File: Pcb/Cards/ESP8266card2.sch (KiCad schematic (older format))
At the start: 13 parts, among them J1 CONN_01X02, J2 CONN_02X06, P1 ESP-Programming-FTDI, U1 SN74AHC1G08, U2 ESP-12E/F, X1 HOLE

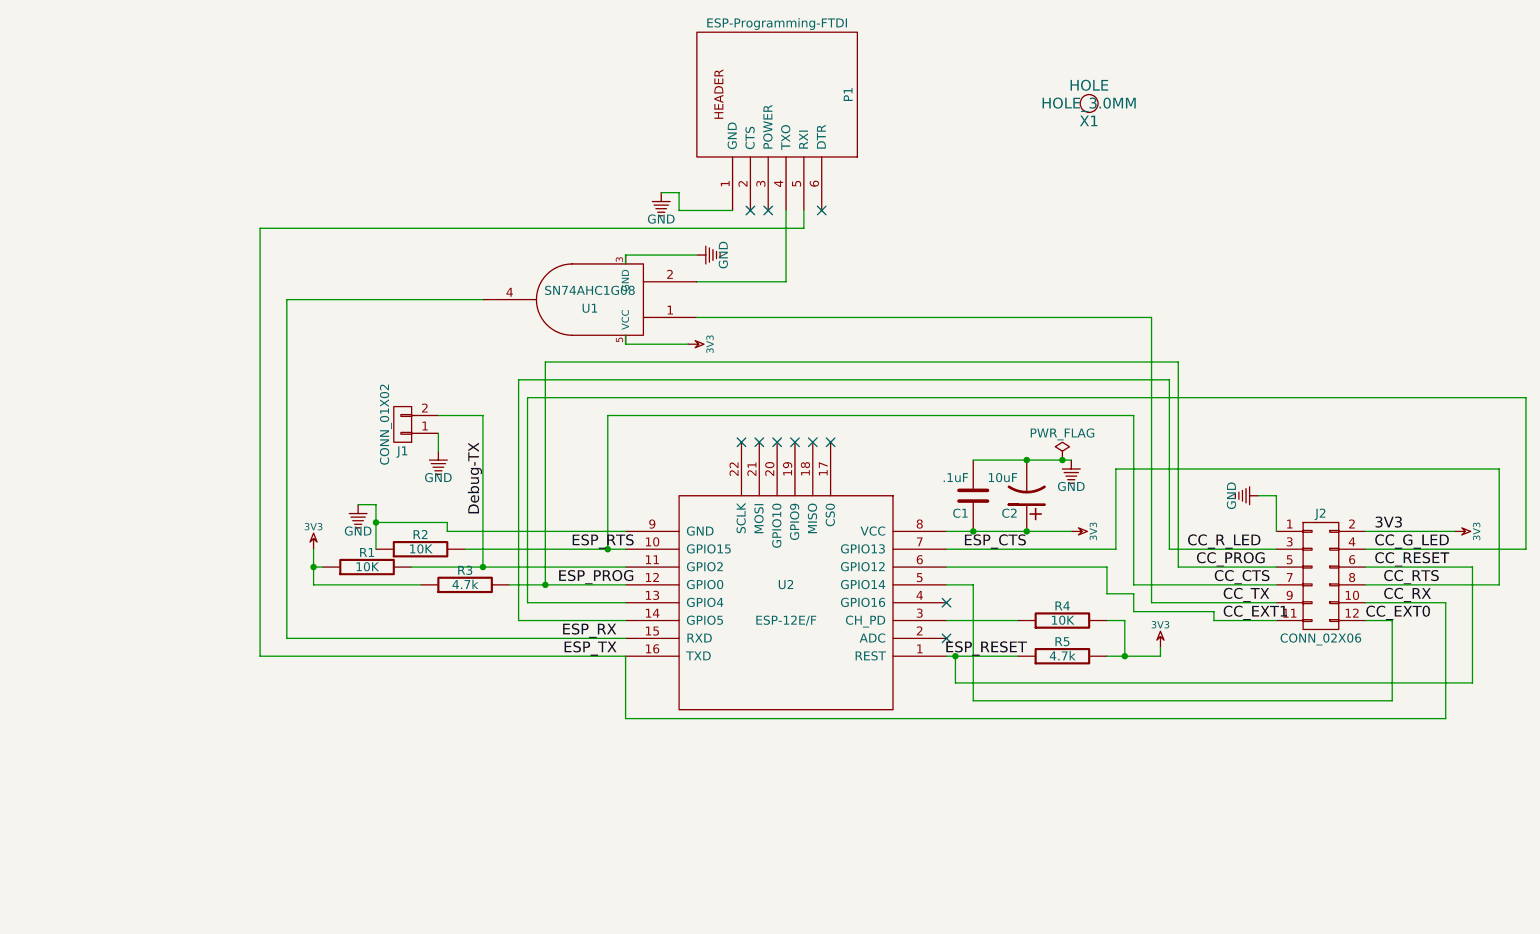
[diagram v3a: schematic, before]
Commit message: Corrected ESP8266card2 for AND gate pins, routing and text.  Added first version of nRF52card.  Put all components in CA6.lib and CA6.pretty   Still needs checking expecially for text.
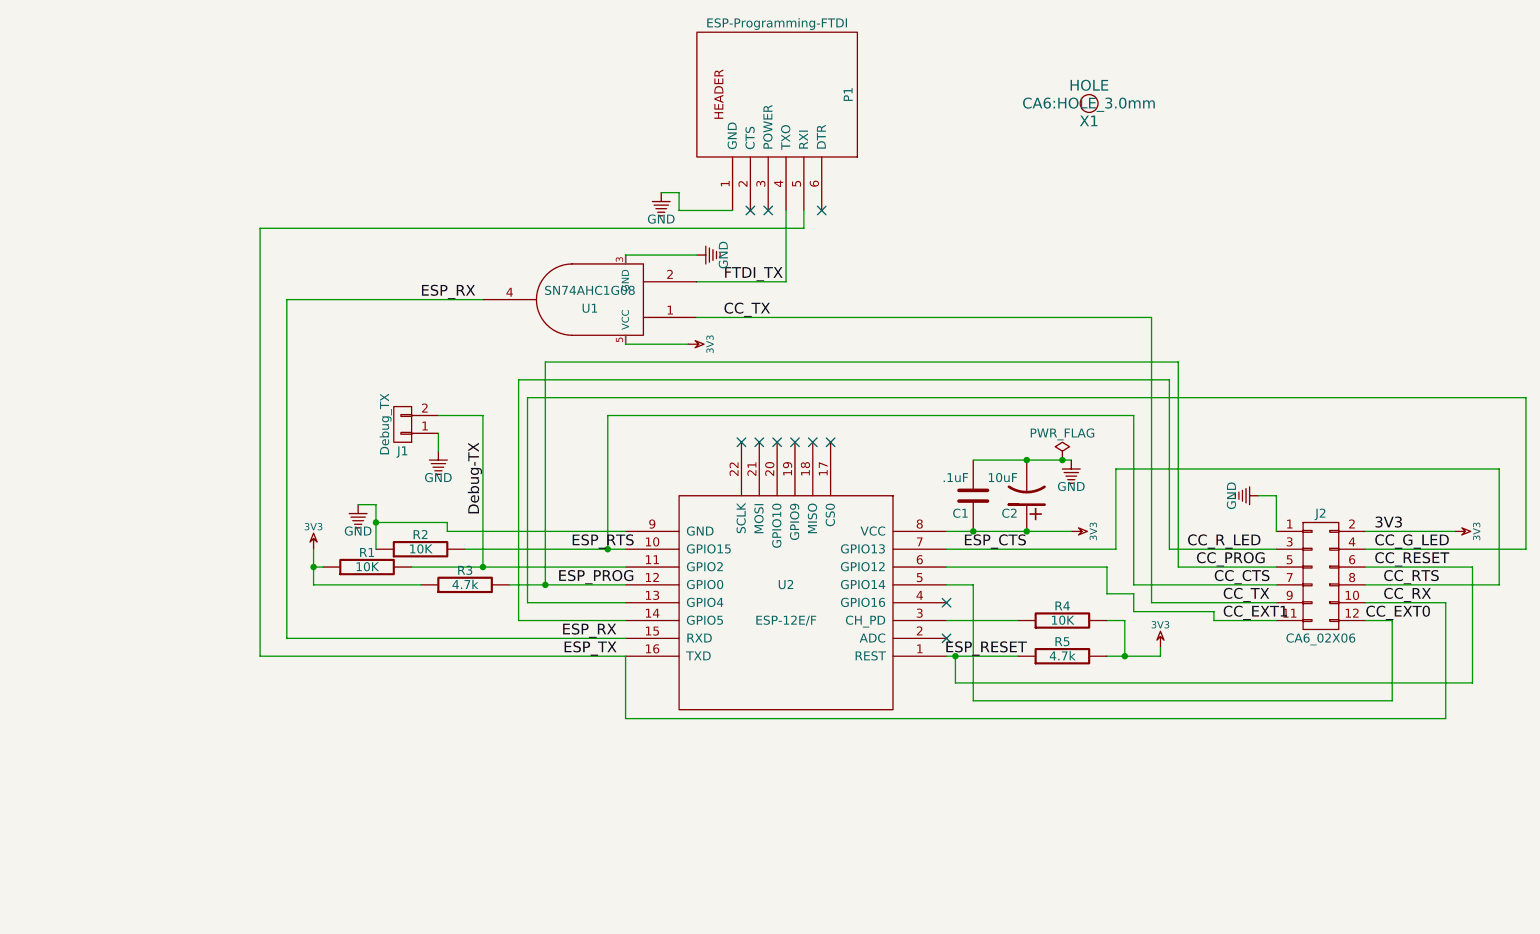
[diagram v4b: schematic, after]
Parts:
- J1: value CONN_01X02 -> Debug_TX; footprint Pin_Headers:Pin_Header_Angled_1x02_Pitch2.54mm -> CA6:Pin_Header_Angled_1x02_Pitch2.54mm
- J2: value CONN_02X06 -> CA6_02X06; footprint Pin_Headers:Pin_Header_Straight_2x06_Pitch2.54mm -> CA6:Pin_Header_Straight_2x06_Pitch2.54mm
- U1: footprint TO_SOT_Packages_SMD:SOT-23-5 -> CA6:SOT-23-5_GATE
- X1: footprint HOLE_3.0MM -> CA6:HOLE_3.0mm
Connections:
- net FTDI_TX: now reaches P1.4 (TXO), U1.2
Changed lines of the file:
@@
 F 0 "U1" H 4650 2900 50  0000 C CNN
 F 1 "SN74AHC1G08" H 4650 2800 50  0000 C CNN
-F 2 "TO_SOT_Packages_SMD:SOT-23-5" H 4600 2600 50  0001 C CNN
+F 2 "CA6:SOT-23-5_GATE" H 4600 2600 50  0001 C CNN
 F 3 "http://www.ti.com/lit/gpn/sn74ahc1g08" H 4650 3250 50  0001 C CNN
 	1    4650 2850
@@
 P 3600 3550
 F 0 "J1" H 3600 3700 50  0000 C CNN
-F 1 "CONN_01X02" V 3700 3550 50  0000 C CNN
-F 2 "Pin_Headers:Pin_Header_Angled_1x02_Pitch2.54mm" H 3600 3550 50  0001 C CNN
+F 1 "Debug_TX" V 3700 3550 50  0000 C CNN
+F 2 "CA6:Pin_Header_Angled_1x02_Pitch2.54mm" H 3600 3550 50  0001 C CNN
 F 3 "" H 3600 3550 50  0001 C CNN
 	1    3600 3550
@@
 P 8750 4400
 F 0 "J2" H 8750 4750 50  0000 C CNN
-F 1 "CONN_02X06" H 8750 4050 50  0000 C CNN
-F 2 "Pin_Headers:Pin_Header_Straight_2x06_Pitch2.54mm" H 8750 3200 50  0001 C CNN
+F 1 "CA6_02X06" H 8750 4050 50  0000 C CNN
+F 2 "CA6:Pin_Header_Straight_2x06_Pitch2.54mm" H 8750 3200 50  0001 C CNN
 F 3 "" H 8750 3200 50  0001 C CNN
 	1    8750 4400
@@
 F 0 "X1" H 7450 1650 60  0000 C CNN
 F 1 "HOLE" H 7450 1850 60  0000 C CNN
-F 2 "HOLE_3.0MM" H 7450 1750 60  0000 C CNN
+F 2 "CA6:HOLE_3.0mm" H 7450 1750 60  0000 C CNN
 F 3 "" H 7450 1750 60  0000 C CNN
 	1    7450 1750
 	1    0    0    -1
 $EndComp
+Text Label 5400 2750 0    60   ~ 0
+FTDI_TX
+Text Label 5400 2950 0    60   ~ 0
+CC_TX
+Text Label 3700 2850 0    60   ~ 0
+ESP_RX
 $EndSCHEMATC
